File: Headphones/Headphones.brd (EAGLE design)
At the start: 50 x 50 mm, 26 parts, among them U1 SI4468, Y1 30MHz

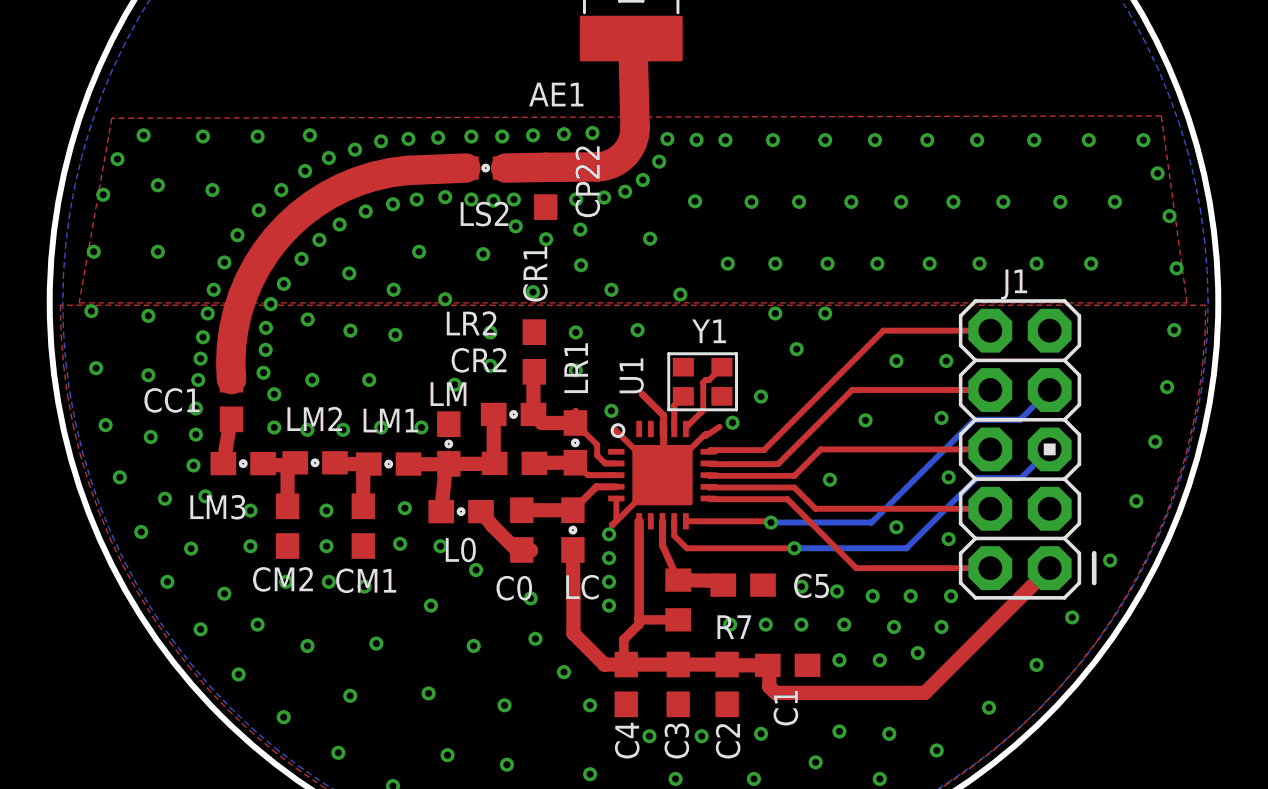
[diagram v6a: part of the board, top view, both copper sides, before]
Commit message: Moved jumper pin names to tNames layer
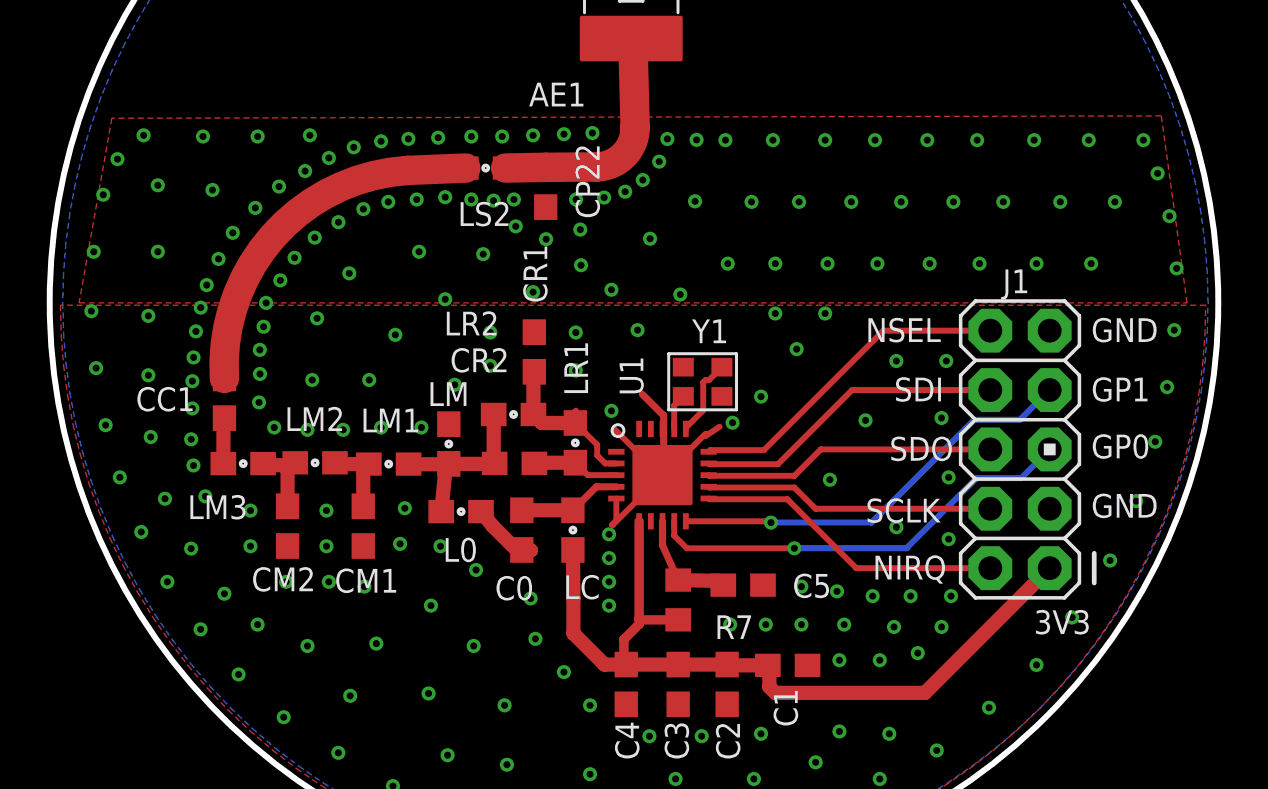
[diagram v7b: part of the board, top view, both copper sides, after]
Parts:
- moved CC1 0.30 mm to (13.5, 18.3)
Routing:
- net GND: vias 214 -> 212
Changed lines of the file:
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@@
 <vertex x="55" y="30.5"/>
 </polygon>
-<text x="41.2496" y="10.5664" size="1.016" layer="51" ratio="14">NIRQ</text>
-<text x="40.9448" y="13.0048" size="1.016" layer="51" ratio="14">SCLK</text>
-<text x="41.9608" y="15.6464" size="1.016" layer="51" ratio="14">SDO</text>
-<text x="42.164" y="18.1864" size="1.016" layer="51" ratio="14">SDI</text>
-<text x="40.9448" y="20.7264" size="1.016" layer="51" ratio="14">NSEL</text>
-<text x="50.5968" y="20.7264" size="1.016" layer="51" ratio="14">GND</text>
-<text x="50.5968" y="13.208" size="1.016" layer="51" ratio="14">GND</text>
-<text x="50.5968" y="15.748" size="1.016" layer="51" ratio="14">GP0</text>
-<text x="50.5968" y="18.1864" size="1.016" layer="51" ratio="14">GP1</text>
-<text x="50.5968" y="9.2456" size="1.016" layer="51" ratio="14" rot="R180">3V3</text>
+<text x="41.2496" y="10.5664" size="1.016" layer="25" ratio="14">NIRQ</text>
+<text x="40.9448" y="13.0048" size="1.016" layer="25" ratio="14">SCLK</text>
+<text x="41.9608" y="15.6464" size="1.016" layer="25" ratio="14">SDO</text>
+<text x="42.164" y="18.1864" size="1.016" layer="25" ratio="14">SDI</text>
+<text x="40.9448" y="20.7264" size="1.016" layer="25" ratio="14">NSEL</text>
+<text x="50.5968" y="20.7264" size="1.016" layer="25" ratio="14">GND</text>
+<text x="50.5968" y="13.208" size="1.016" layer="25" ratio="14">GND</text>
+<text x="50.5968" y="15.748" size="1.016" layer="25" ratio="14">GP0</text>
+<text x="50.5968" y="18.1864" size="1.016" layer="25" ratio="14">GP1</text>
+<text x="50.5968" y="9.2456" size="1.016" layer="25" ratio="14" rot="R180">3V3</text>
 </plain>
 <attributes>
@@
 <attribute name="NAME" x="39.4918" y="10.8026" size="1.016" layer="25" ratio="14" rot="R180"/>
 </element>
-<element name="CC1" library="resistor" package="C0603" value="56pF" x="13.817" y="18.267" locked="yes" smashed="yes" rot="R270">
-<attribute name="NAME" x="10.0212" y="17.72" size="1.016" layer="25" ratio="14"/>
+<element name="CC1" library="resistor" package="C0603" value="56pF" x="13.517" y="18.317" smashed="yes" rot="R270">
+<attribute name="NAME" x="9.7212" y="17.77" size="1.016" layer="25" ratio="14"/>
 </element>
 <element name="CM2" library="resistor" package="C0603" value="4.7pF" x="16.218" y="12.848" locked="yes" smashed="yes" rot="R90">
@@
 </polygon>
 <wire x1="34.1" y1="16.7" x2="34.7" y2="17.1" width="0.254" layer="1"/>
-<via x="15.1884" y="19.4088" extent="1-16" drill="0.3"/>
-<via x="15.2916" y="21.3296" extent="1-16" drill="0.3"/>
-<via x="15.498" y="22.3472" extent="1-16" drill="0.3"/>
-<via x="16.0576" y="23.2132" extent="1-16" drill="0.3"/>
-<via x="16.8172" y="24.2792" extent="1-16" drill="0.3"/>
-<via x="17.58" y="25.092" extent="1-16" drill="0.3"/>
-<via x="18.4444" y="25.7532" extent="1-16" drill="0.3"/>
-<via x="19.5604" y="26.3128" extent="1-16" drill="0.3"/>
-<via x="20.7264" y="26.6192" extent="1-16" drill="0.3"/>
+<via x="15.0384" y="19.3588" extent="1-16" drill="0.3"/>
+<via x="15.1916" y="21.3796" extent="1-16" drill="0.3"/>
+<via x="15.298" y="22.3972" extent="1-16" drill="0.3"/>
+<via x="15.9076" y="23.3632" extent="1-16" drill="0.3"/>
+<via x="16.5172" y="24.3292" extent="1-16" drill="0.3"/>
+<via x="17.38" y="25.192" extent="1-16" drill="0.3"/>
+<via x="18.3944" y="25.8532" extent="1-16" drill="0.3"/>
+<via x="19.4604" y="26.4128" extent="1-16" drill="0.3"/>
+<via x="20.5264" y="26.7192" extent="1-16" drill="0.3"/>
 <via x="21.7424" y="26.8224" extent="1-16" drill="0.3"/>
 <via x="22.9616" y="26.924" extent="1-16" drill="0.3"/>
@@
 <via x="29.972" y="10.4648" extent="1-16" drill="0.3"/>
 <via x="29.972" y="9.4488" extent="1-16" drill="0.3"/>
-<wire x1="26.7208" y1="26.924" x2="26.7208" y2="26.924" width="0" layer="19" extent="1-16"/>
-<wire x1="28.0416" y1="26.924" x2="28.0416" y2="26.924" width="0" layer="19" extent="1-16"/>
 <via x="28.5608" y="26.824" extent="1-16" drill="0.3"/>
 <via x="29.2608" y="29.6672" extent="1-16" drill="0.3"/>
@@
 <via x="21.3876" y="29.4156" extent="1-16" drill="0.3"/>
 <via x="20.2184" y="29.3124" extent="1-16" drill="0.3"/>
-<via x="19.1008" y="28.956" extent="1-16" drill="0.3"/>
+<via x="19.0508" y="29.056" extent="1-16" drill="0.3"/>
 <via x="17.9848" y="28.5996" extent="1-16" drill="0.3"/>
 <via x="16.9672" y="28.04" extent="1-16" drill="0.3"/>
-<via x="15.9512" y="27.2272" extent="1-16" drill="0.3"/>
-<via x="14.9868" y="26.3628" extent="1-16" drill="0.3"/>
-<via x="14.074" y="25.2968" extent="1-16" drill="0.3"/>
-<via x="13.5144" y="24.1292" extent="1-16" drill="0.3"/>
-<via x="13.058" y="22.9616" extent="1-16" drill="0.3"/>
-<via x="12.8016" y="21.9456" extent="1-16" drill="0.3"/>
-<via x="12.5984" y="20.9296" extent="1-16" drill="0.3"/>
-<via x="12.4968" y="20.0152" extent="1-16" drill="0.3"/>
-<via x="12.3952" y="19.1008" extent="1-16" drill="0.3"/>
+<via x="15.8512" y="27.3772" extent="1-16" drill="0.3"/>
+<via x="14.8368" y="26.4628" extent="1-16" drill="0.3"/>
+<via x="13.874" y="25.3968" extent="1-16" drill="0.3"/>
+<via x="13.2644" y="24.2792" extent="1-16" drill="0.3"/>
+<via x="12.758" y="23.1616" extent="1-16" drill="0.3"/>
+<via x="12.5016" y="22.1956" extent="1-16" drill="0.3"/>
+<via x="12.2984" y="21.1796" extent="1-16" drill="0.3"/>
+<via x="12.1968" y="20.0652" extent="1-16" drill="0.3"/>
+<via x="12.1452" y="19.0508" extent="1-16" drill="0.3"/>
 <via x="35.2552" y="17.272" extent="1-16" drill="0.3"/>
 <via x="30.0736" y="17.78" extent="1-16" drill="0.3"/>
@@
 <via x="20.2184" y="17.0688" extent="1-16" drill="0.3"/>
 <via x="15.6464" y="17.0688" extent="1-16" drill="0.3"/>
-<via x="15.6464" y="18.4912" extent="1-16" drill="0.3"/>
+<via x="14.9964" y="18.1412" extent="1-16" drill="0.3"/>
 <via x="17.0688" y="16.9672" extent="1-16" drill="0.3"/>
 <via x="18.5928" y="16.9672" extent="1-16" drill="0.3"/>
@@
 <via x="21.844" y="24.5872" extent="1-16" drill="0.3"/>
 <via x="18.8572" y="23.6632" extent="1-16" drill="0.3"/>
-<via x="17.08" y="21.6892" extent="1-16" drill="0.3"/>
+<via x="17.48" y="21.7392" extent="1-16" drill="0.3"/>
 <via x="17.272" y="19.1008" extent="1-16" drill="0.3"/>
 <via x="19.7104" y="19.1008" extent="1-16" drill="0.3"/>
@@
 <via x="10.2616" y="21.844" extent="1-16" drill="0.3"/>
 <via x="10.2616" y="19.304" extent="1-16" drill="0.3"/>
-<via x="12.2936" y="17.8816" extent="1-16" drill="0.3"/>
-<via x="12.2936" y="16.764" extent="1-16" drill="0.3"/>
+<via x="12.1436" y="17.8816" extent="1-16" drill="0.3"/>
+<via x="12.0936" y="16.564" extent="1-16" drill="0.3"/>
 <via x="12.192" y="15.4432" extent="1-16" drill="0.3"/>
 <via x="12.7" y="14.1224" extent="1-16" drill="0.3"/>
@@
 <via x="41.9608" y="3.9624" extent="1-16" drill="0.3"/>
 <via x="39.8272" y="4.064" extent="1-16" drill="0.3"/>
-<wire x1="34.1" y1="16.7" x2="34.1" y2="16.8" width="0" layer="19" extent="1-1"/>
-<wire x1="32.259" y1="17.005" x2="32.3088" y2="17.5768" width="0" layer="19" extent="1-1"/>
 <via x="30.6608" y="27.1564" extent="1-16" drill="0.3"/>
 <via x="25.0292" y="26.774" extent="1-16" drill="0.3"/>
@@
 <via x="27.2792" y="25.124" extent="1-16" drill="0.3"/>
 <via x="28.7736" y="24.0116" extent="1-16" drill="0.3"/>
-<via x="15.28" y="20.3892" extent="1-16" drill="0.3"/>
-<via x="20.7572" y="22.9632" extent="1-16" drill="0.3"/>
-<via x="18.9072" y="21.2132" extent="1-16" drill="0.3"/>
+<via x="15.03" y="20.3892" extent="1-16" drill="0.3"/>
+<wire x1="34.1" y1="16.7" x2="34.1" y2="16.8" width="0" layer="19" extent="1-1"/>
+<wire x1="32.259" y1="17.005" x2="32.3088" y2="17.5768" width="0" layer="19" extent="1-1"/>
 </signal>
 <signal name="N$7">
@@
 <contactref element="LM3" pad="1"/>
 <contactref element="CC1" pad="2"/>
-<wire x1="13.4712" y1="15.523" x2="13.776" y2="17.376" width="0.6096" layer="1"/>
-<wire x1="13.776" y1="17.376" x2="13.817" y2="17.417" width="0.6096" layer="1"/>
+<wire x1="13.4712" y1="15.523" x2="13.476" y2="17.326" width="0.6096" layer="1"/>
+<wire x1="13.476" y1="17.326" x2="13.517" y2="17.467" width="0.6096" layer="1"/>
 </signal>
 <signal name="N$3">
@@
 <contactref element="LS2" pad="2"/>
 <contactref element="CC1" pad="1"/>
-<wire x1="13.817" y1="19.117" x2="21.3444" y2="28.0668" width="1.26" layer="1" curve="-90"/>
+<wire x1="13.517" y1="19.167" x2="21.3444" y2="28.0668" width="1.26" layer="1" curve="-90"/>
 <wire x1="21.3444" y1="28.0668" x2="23.8442" y2="28.1684" width="1.26" layer="1"/>
 </signal>
